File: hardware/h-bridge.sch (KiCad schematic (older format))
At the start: 24 parts

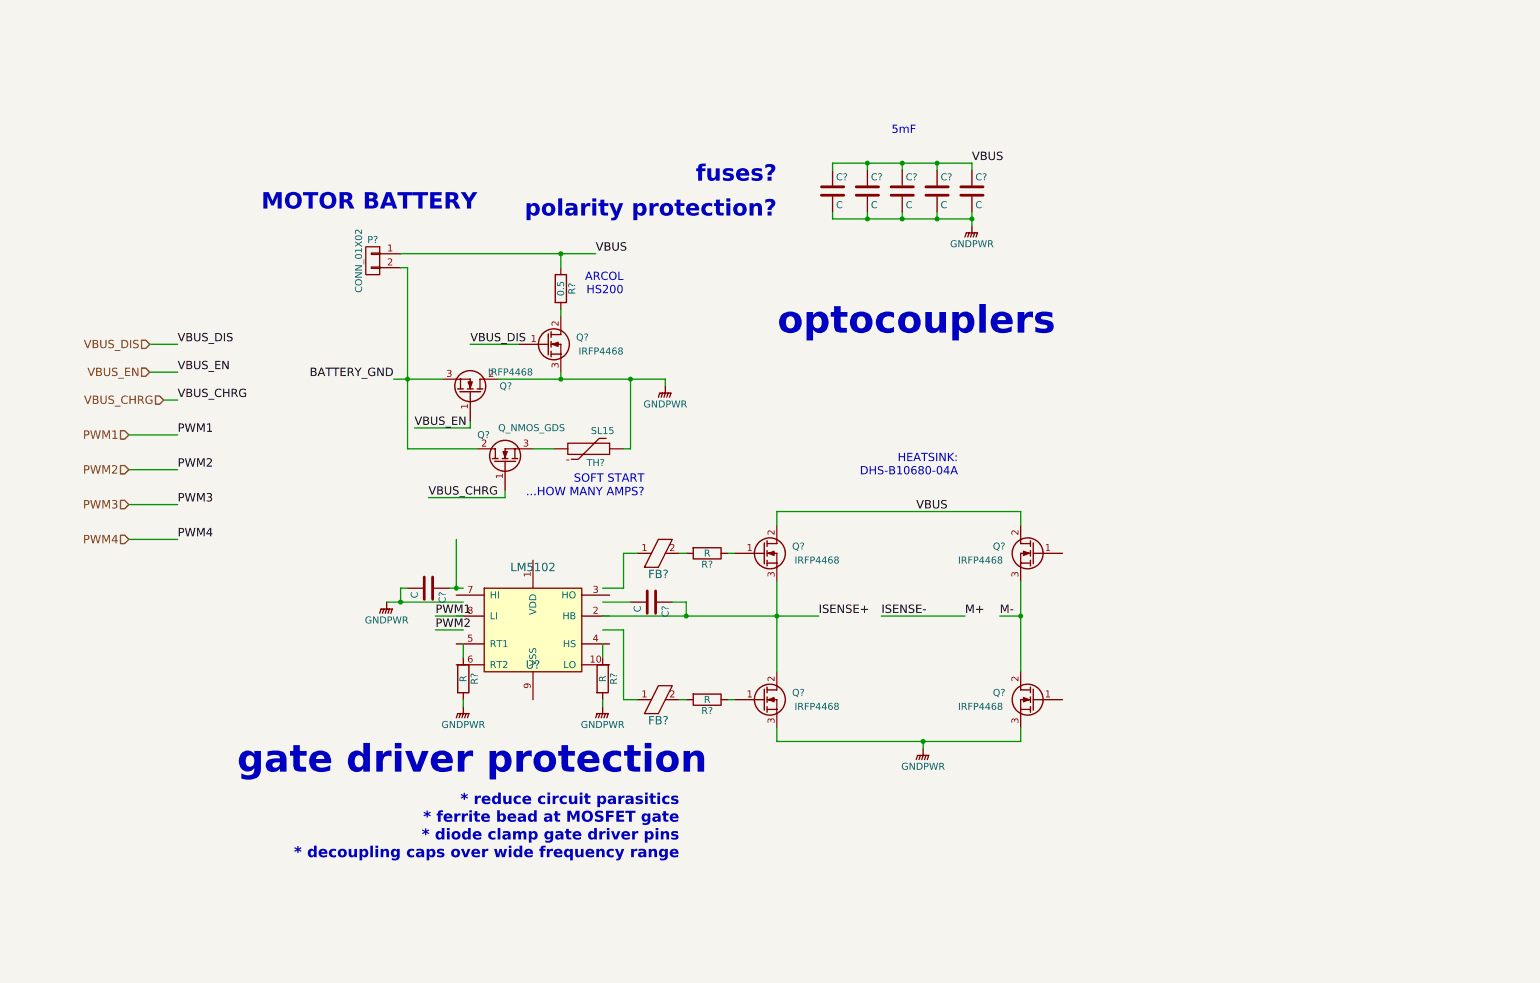
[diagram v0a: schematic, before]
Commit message: cleaned up h-bridge; added digital isolators
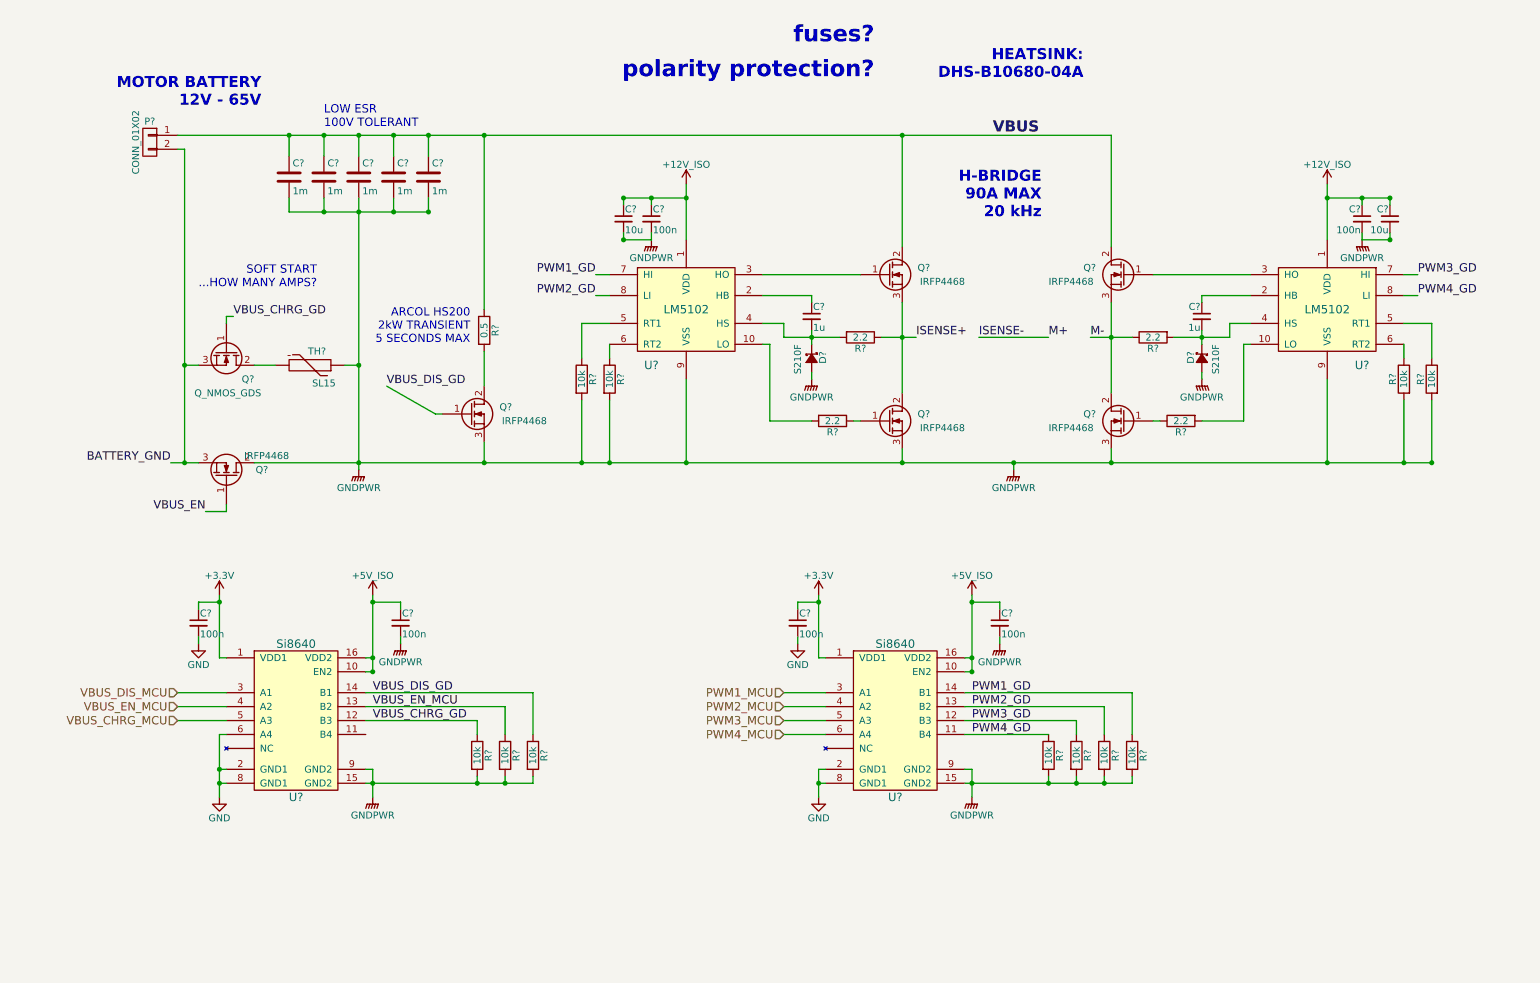
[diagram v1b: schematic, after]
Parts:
- removed C? (x7): C, symbol C
- removed FB? (x2): FERRITE_BEAD, symbol FERRITE_BEAD
- removed R? (x3): R, symbol R
- removed U?: LM5102, symbol LM5102
- added C? (x2): 1u, symbol C_Small
- added C? (x6): 100n, symbol C_Small
- added C? (x2): 10u, symbol C_Small
- added C? (x5): 1m, symbol C
- added D? (x2): S210F, symbol D_Schottky_Small
- added R? (x11): 10k, symbol R
- added R? (x3): 2.2, symbol R
- added U? (x2): Si8640, symbol Si8640
- added U? (x2): LM5102, symbol LM5102
- R?: value R -> 2.2
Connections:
- net labels added: +12V_ISO, +3.3V, +5V_ISO, GND, PWM1_GD, PWM1_MCU, PWM2_GD, PWM2_MCU, PWM3_GD, PWM3_MCU, PWM4_GD, PWM4_MCU, VBUS_CHRG_GD, VBUS_CHRG_MCU, VBUS_DIS_GD, VBUS_DIS_MCU, VBUS_EN_MCU
- net labels removed: PWM1, PWM2, PWM3, PWM4, VBUS_CHRG, VBUS_DIS
- wire segments 73 -> 156
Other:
- note added: "ARCOL HS200\n2kW TRANSIENT\n5 SECONDS MAX"
- note added: "H-BRIDGE\n90A MAX\n20 kHz"
- note added: "LOW ESR\n100V TOLERANT"
- note added: "MOTOR BATTERY\n12V - 65V"
- note removed: "* reduce circuit parasitics\n* ferrite bead at MOSFET gate\n* diode clamp gate driver pins\n* decoupling caps over wide frequency range"
- note removed: "5mF"
- note removed: "ARCOL\nHS200"
- note removed: "MOTOR BATTERY"
- note removed: "gate driver protection"
- note removed: "optocouplers"
- moved on the sheet: P?, Q?, R?, TH?

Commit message: improved inrush limiter, isolator, added aux. gate drive
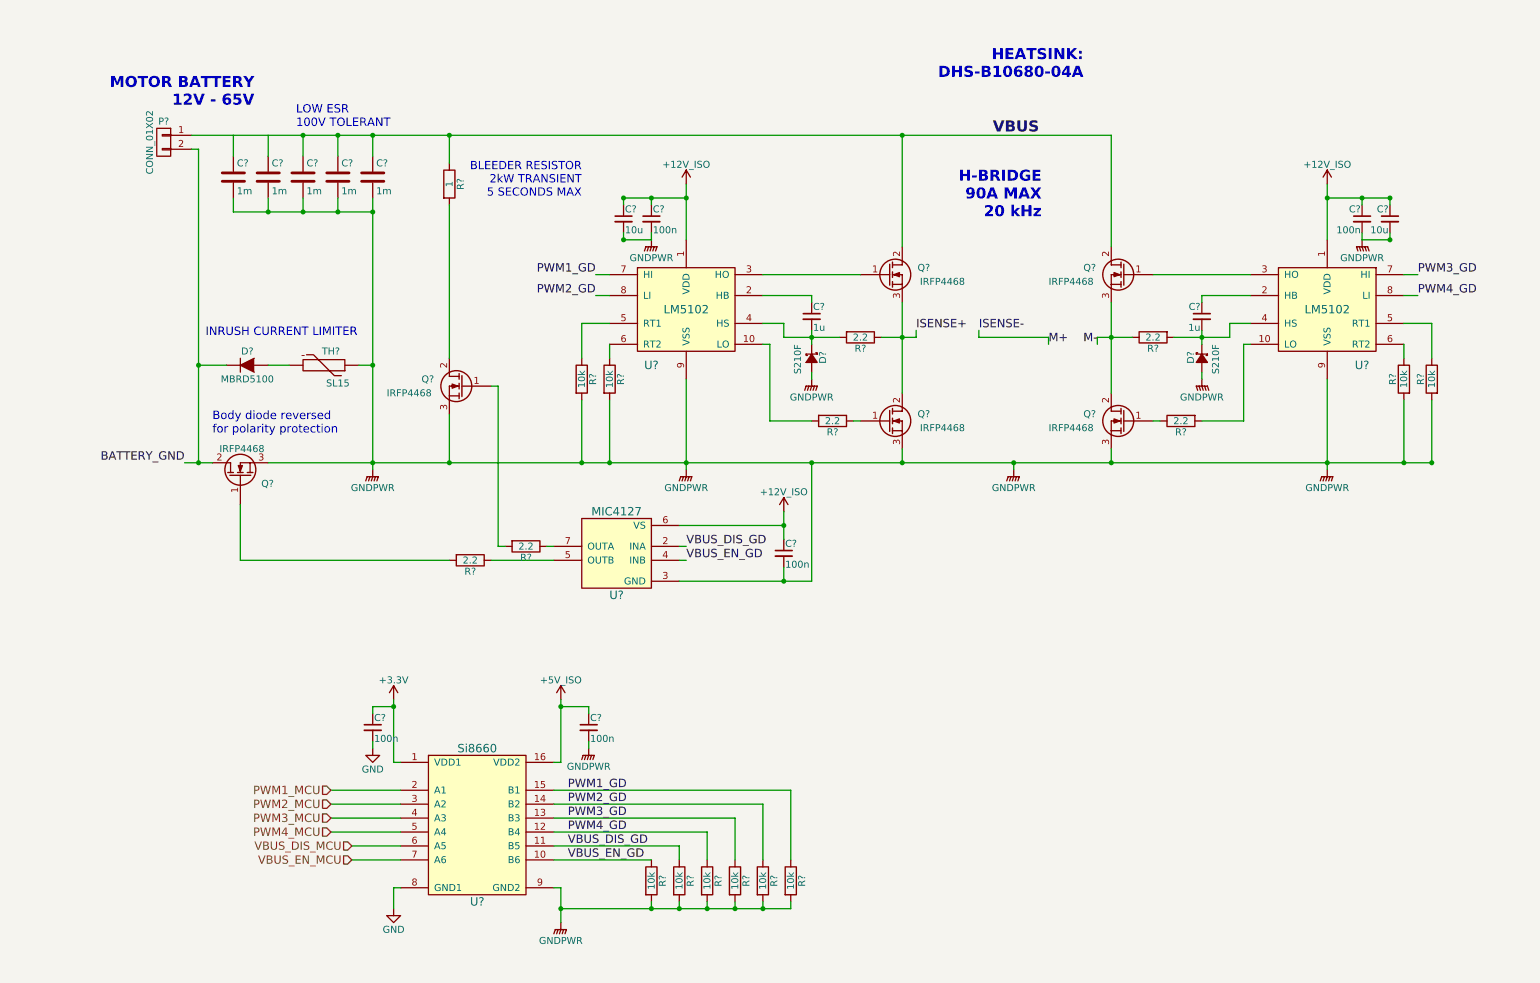
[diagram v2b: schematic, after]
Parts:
- removed C? (x2): 100n, symbol C_Small
- removed Q?: Q_NMOS_GDS, symbol Q_NMOS_GDS
- removed R? (x3): 10k, symbol R
- removed U? (x2): Si8640, symbol Si8640
- added C?: 100n, symbol C_Small
- added D?: MBRD5100, symbol D
- added R? (x2): 2.2, symbol R
- added R? (x2): 10k, symbol R
- added U?: MIC4127, symbol MIC4127
- added U?: Si8660, symbol Si8660
- R?: value 0.5 -> 1
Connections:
- net +12V_ISO: now also C?.1, U?.6 (VS)
- net +3V3: now also U?.1 (VDD1)
- net +5V_ISO: now also U?.16 (VDD2)
- net BATTERY_GND: now also Q?.2 (D), D?.1 (K); no longer Q?.3 (S)
- net GND: now also U?.8 (GND1)
- net GNDPWR: now also Q?.3 (S), C?.2, R?.2, R?.2, U?.3 (GND), U?.9 (GND2); no longer Q?.2 (D)
- net PWM1_GD: now also R?.1, U?.15 (B1); no longer R?.1
- net PWM1_MCU: now also U?.2 (A1)
- net PWM2_GD: now also R?.1, U?.14 (B2); no longer R?.1
- net PWM2_MCU: now also U?.3 (A2)
- net PWM3_GD: now also R?.1, U?.13 (B3); no longer R?.1
- net PWM3_MCU: now also U?.4 (A3)
- net PWM4_GD: now also R?.1, U?.12 (B4); no longer R?.1
- net PWM4_MCU: now also U?.5 (A4)
- net VBUS: no longer C?.1, C?.1
- net VBUS_DIS_GD: now also R?.1, U?.11 (B5), U?.2 (INA); no longer Q?.1 (G)
- net VBUS_DIS_MCU: now also U?.6 (A5)
- net VBUS_EN_MCU: now also U?.7 (A6)
- net at TH?.2: now also D?.2 (A)
- net VBUS_EN: no longer names the net of Q?.1 (G)
- net VBUS_EN: now also R?.2
- new net: Q?.1 (G), R?.2
- new net: R?.1, U?.5 (OUTB)
- new net: R?.1, U?.7 (OUTA)
- new net VBUS_EN_GD: R?.1, U?.10 (B6), U?.4 (INB)
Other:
- note added: "BLEEDER RESISTOR\n2kW TRANSIENT\n5 SECONDS MAX"
- note added: "Body diode reversed\nfor polarity protection"
- note added: "INRUSH CURRENT LIMITER"
- note removed: "ARCOL HS200\n2kW TRANSIENT\n5 SECONDS MAX"
- note removed: "SOFT START\n...HOW MANY AMPS?"
- note removed: "fuses?"
- note removed: "polarity protection?"
- moved on the sheet: C?, P?, Q?, R?, TH?

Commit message: ERC cleanup, begin pcbnew population
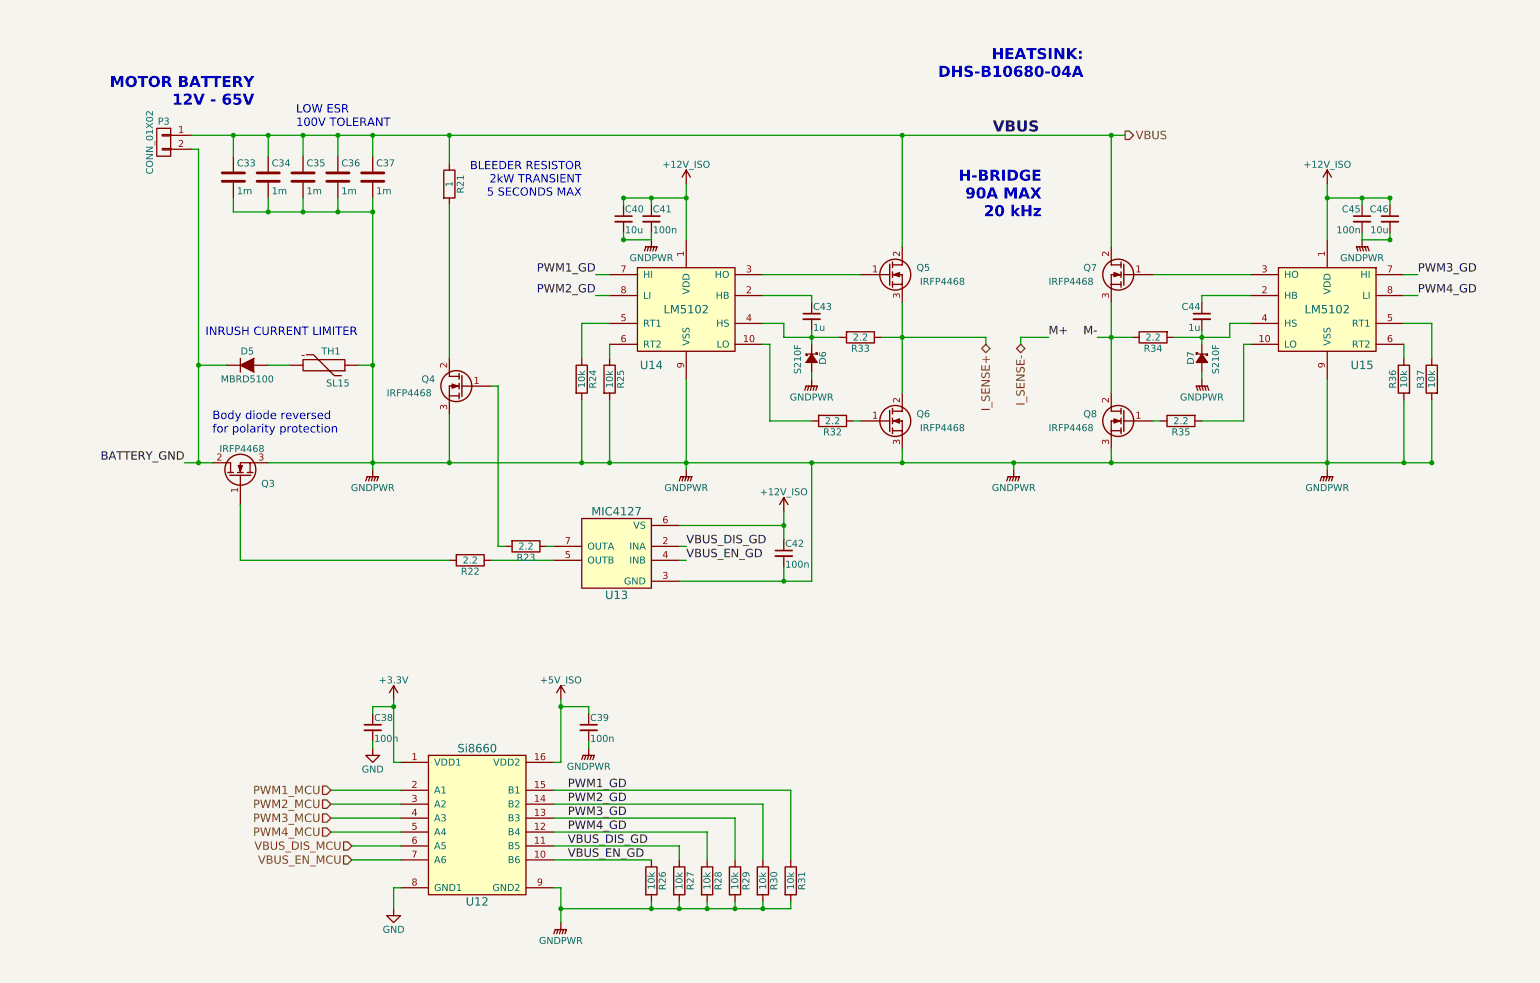
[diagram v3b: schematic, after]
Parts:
- C33, C34, C35, C36, C37: renamed from C?; footprint (none) -> Capacitors_ThroughHole:C_Radial_D18_L36_P7.5
- C38, C39, C40, C41, C42, C43, C44, C45, C46: renamed from C?; footprint (none) -> Capacitors_SMD:C_0603
- D5: renamed from D?; footprint (none) -> TO_SOT_Packages_SMD:TO-263-3Lead
- D6, D7: renamed from D?; footprint (none) -> Diodes_SMD:SOD-123
- Q3, Q4, Q5, Q6, Q7, Q8: renamed from Q?; footprint (none) -> TO_SOT_Packages_THT:TO-247_Horizontal_Neutral123_MountFromLS_largePads
- R21, R22, R23, R24, R25, R26, R27, R28, R29, R30, R31, R32, R33, R34, R35, R36, R37: renamed from R?; footprint (none) -> Resistors_SMD:R_0603
- U12: renamed from U?; footprint (none) -> Housings_SOIC:SOIC-16_3.9x9.9mm_Pitch1.27mm
- U14, U15: renamed from U?; footprint (none) -> Housings_SSOP:MSOP-10_3x3mm_Pitch0.5mm
- gave numbers to parts that had none: 3
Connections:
- net VBUS: now also C33.1, C34.1
- net ISENSE+ renamed I_SENSE+

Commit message: hw: minor tweaks
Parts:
- TH1: value SL15 -> B57213P0470; footprint (none) -> Resistors_ThroughHole:Resistor_Vertical_RM7.5mm
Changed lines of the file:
@@
 $EndComp
 $Comp
-L GNDPWR #PWR058
+L GNDPWR #PWR059
 U 1 1 5975827F
 P 7500 3850
-F 0 "#PWR058" H 7500 3650 50  0001 C CNN
+F 0 "#PWR059" H 7500 3650 50  0001 C CNN
 F 1 "GNDPWR" H 7500 3720 50  0000 C CNN
 F 2 "" H 7500 3800 50  0000 C CNN
@@
 P 2550 3100
 F 0 "TH1" V 2650 3150 50  0000 C CNN
-F 1 "SL15" V 2450 3200 50  0000 C BNN
-F 2 "" H 2550 3100 50  0001 C CNN
+F 1 "B57213P0470" V 2450 3150 50  0000 C BNN
+F 2 "Resistors_ThroughHole:Resistor_Vertical_RM7.5mm" H 2550 3100 50  0001 C CNN
 F 3 "" H 2550 3100 50  0000 C CNN
 	1    2550 3100
@@
 $EndComp
 $Comp
-L GNDPWR #PWR059
+L GNDPWR #PWR060
 U 1 1 59959CCF
 P 4900 2200
-F 0 "#PWR059" H 4900 2000 50  0001 C CNN
+F 0 "#PWR060" H 4900 2000 50  0001 C CNN
 F 1 "GNDPWR" H 4900 2070 50  0000 C CNN
 F 2 "" H 4900 2150 50  0000 C CNN
@@
 $EndComp
 $Comp
-L +12V_ISO #PWR060
+L +12V_ISO #PWR061
 U 1 1 5995F515
 P 5150 1800
-F 0 "#PWR060" H 5150 1650 50  0001 C CNN
+F 0 "#PWR061" H 5150 1650 50  0001 C CNN
 F 1 "+12V_ISO" H 5150 1940 50  0000 C CNN
 F 2 "" H 5150 1800 50  0000 C CNN
@@
 $EndComp
 $Comp
-L GNDPWR #PWR061
+L GNDPWR #PWR062
 U 1 1 5998917B
 P 10000 2200
-F 0 "#PWR061" H 10000 2000 50  0001 C CNN
+F 0 "#PWR062" H 10000 2000 50  0001 C CNN
 F 1 "GNDPWR" H 10000 2070 50  0000 C CNN
 F 2 "" H 10000 2150 50  0000 C CNN
@@
 $EndComp
 $Comp
-L +12V_ISO #PWR062
+L +12V_ISO #PWR063
 U 1 1 59989187
 P 9750 1800
-F 0 "#PWR062" H 9750 1650 50  0001 C CNN
+F 0 "#PWR063" H 9750 1650 50  0001 C CNN
 F 1 "+12V_ISO" H 9750 1940 50  0000 C CNN
 F 2 "" H 9750 1800 50  0000 C CNN
@@
 $EndComp
 $Comp
-L GNDPWR #PWR063
+L GNDPWR #PWR064
 U 1 1 599891AB
 P 8850 3200
-F 0 "#PWR063" H 8850 3000 50  0001 C CNN
+F 0 "#PWR064" H 8850 3000 50  0001 C CNN
 F 1 "GNDPWR" H 8850 3070 50  0000 C CNN
 F 2 "" H 8850 3150 50  0000 C CNN
@@
 $EndComp
 $Comp
-L GNDPWR #PWR064
+L GNDPWR #PWR065
 U 1 1 59967530
 P 6050 3200
-F 0 "#PWR064" H 6050 3000 50  0001 C CNN
+F 0 "#PWR065" H 6050 3000 50  0001 C CNN
 F 1 "GNDPWR" H 6050 3070 50  0000 C CNN
 F 2 "" H 6050 3150 50  0000 C CNN
@@
 LOW ESR\n100V TOLERANT
 $Comp
-L GNDPWR #PWR065
+L GNDPWR #PWR066
 U 1 1 599BCA83
 P 2900 3850
-F 0 "#PWR065" H 2900 3650 50  0001 C CNN
+F 0 "#PWR066" H 2900 3650 50  0001 C CNN
 F 1 "GNDPWR" H 2900 3720 50  0000 C CNN
 F 2 "" H 2900 3800 50  0000 C CNN
@@
 $EndComp
 $Comp
-L +3.3V #PWR066
+L +3.3V #PWR067
 U 1 1 599D3CAE
 P 3050 5500
-F 0 "#PWR066" H 3050 5350 50  0001 C CNN
+F 0 "#PWR067" H 3050 5350 50  0001 C CNN
 F 1 "+3.3V" H 3050 5640 50  0000 C CNN
 F 2 "" H 3050 5500 50  0000 C CNN
@@
 $EndComp
 $Comp
-L GND #PWR067
+L GND #PWR068
 U 1 1 599D3CC0
 P 2900 5850
-F 0 "#PWR067" H 2900 5600 50  0001 C CNN
+F 0 "#PWR068" H 2900 5600 50  0001 C CNN
 F 1 "GND" H 2900 5700 50  0000 C CNN
 F 2 "" H 2900 5850 50  0000 C CNN
@@
 $EndComp
 $Comp
-L +5V_ISO #PWR068
+L +5V_ISO #PWR069
 U 1 1 599D3CD5
 P 4250 5500
-F 0 "#PWR068" H 4250 5350 50  0001 C CNN
+F 0 "#PWR069" H 4250 5350 50  0001 C CNN
 F 1 "+5V_ISO" H 4250 5640 50  0000 C CNN
 F 2 "" H 4250 5500 50  0000 C CNN
@@
 $EndComp
 $Comp
-L GNDPWR #PWR069
+L GNDPWR #PWR070
 U 1 1 599D3CF4
 P 4450 5850
-F 0 "#PWR069" H 4450 5650 50  0001 C CNN
+F 0 "#PWR070" H 4450 5650 50  0001 C CNN
 F 1 "GNDPWR" H 4450 5720 50  0000 C CNN
 F 2 "" H 4450 5800 50  0000 C CNN
@@
 	5100 4650 6050 4650
 $Comp
-L +12V_ISO #PWR070
+L +12V_ISO #PWR071
 U 1 1 59A0BCFD
 P 5850 4150
-F 0 "#PWR070" H 5850 4000 50  0001 C CNN
+F 0 "#PWR071" H 5850 4000 50  0001 C CNN
 F 1 "+12V_ISO" H 5850 4290 50  0000 C CNN
 F 2 "" H 5850 4150 50  0000 C CNN
@@
 	1950 4500 3450 4500
 $Comp
-L GNDPWR #PWR071
+L GNDPWR #PWR072
 U 1 1 59A194F2
 P 5150 3850
-F 0 "#PWR071" H 5150 3650 50  0001 C CNN
+F 0 "#PWR072" H 5150 3650 50  0001 C CNN
 F 1 "GNDPWR" H 5150 3720 50  0000 C CNN
 F 2 "" H 5150 3800 50  0000 C CNN
@@
 $EndComp
 $Comp
-L GNDPWR #PWR072
+L GNDPWR #PWR073
 U 1 1 59A199E4
 P 9750 3850
-F 0 "#PWR072" H 9750 3650 50  0001 C CNN
+F 0 "#PWR073" H 9750 3650 50  0001 C CNN
 F 1 "GNDPWR" H 9750 3720 50  0000 C CNN
 F 2 "" H 9750 3800 50  0000 C CNN
@@
 $EndComp
 $Comp
-L GND #PWR073
+L GND #PWR074
 U 1 1 59A2238F
 P 3050 7000
-F 0 "#PWR073" H 3050 6750 50  0001 C CNN
+F 0 "#PWR074" H 3050 6750 50  0001 C CNN
 F 1 "GND" H 3050 6850 50  0000 C CNN
 F 2 "" H 3050 7000 50  0000 C CNN
@@
 $EndComp
 $Comp
-L GNDPWR #PWR074
+L GNDPWR #PWR075
 U 1 1 59A24543
 P 4250 7100
-F 0 "#PWR074" H 4250 6900 50  0001 C CNN
+F 0 "#PWR075" H 4250 6900 50  0001 C CNN
 F 1 "GNDPWR" H 4250 6970 50  0000 C CNN
 F 2 "" H 4250 7050 50  0000 C CNN
